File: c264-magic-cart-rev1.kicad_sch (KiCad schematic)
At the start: 10 parts, among them CN1 C16_NEWSTYLE_EXP_PORT, U1 27C080, U2 74HCT273, U3 27C160, U5 GAL20V8

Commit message: Add cap for U3
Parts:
- added C3: 100n, Capacitor_THT:C_Disc_D7.5mm_W2.5mm_P5.00mm, symbol Device:C
- renumbered C2 to C1, C3 to C2
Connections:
- net GND: now also C3.2
- net VCC: now also C3.1
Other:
- moved on the sheet: C2
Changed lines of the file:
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@@
 	)
 	(junction
-		(at 218.44 127)
+		(at 46.99 175.26)
 		(diameter 0)
 		(color 0 0 0 0)
 	)
 	(junction
-		(at 88.9 177.8)
+		(at 218.44 127)
 		(diameter 0)
 		(color 0 0 0 0)
 	)
 	(junction
-		(at 35.56 175.26)
+		(at 46.99 167.64)
 		(diameter 0)
 		(color 0 0 0 0)
 	)
 	(junction
-		(at 49.53 175.26)
+		(at 88.9 177.8)
 		(diameter 0)
 		(color 0 0 0 0)
 	)
 	(junction
-		(at 49.53 167.64)
+		(at 35.56 175.26)
 		(diameter 0)
 		(color 0 0 0 0)
@@
 	(wire
 		(pts
-			(xy 35.56 175.26) (xy 49.53 175.26)
+			(xy 46.99 167.64) (xy 49.53 167.64)
+		)
+		(stroke
+			(width 0)
+			(type default)
+		)
+	)
+	(wire
+		(pts
+			(xy 35.56 175.26) (xy 46.99 175.26)
 		)
 		(stroke
@@
 	(wire
 		(pts
-			(xy 49.53 175.26) (xy 54.61 175.26)
-		)
-		(stroke
-			(width 0.1524)
-			(type solid)
-		)
-	)
-	(wire
-		(pts
 			(xy 81.28 113.03) (xy 83.82 113.03)
 		)
@@
 	(wire
 		(pts
-			(xy 49.53 167.64) (xy 54.61 167.64)
+			(xy 49.53 167.64) (xy 58.42 167.64)
 		)
 		(stroke
@@
 	(wire
 		(pts
-			(xy 35.56 167.64) (xy 49.53 167.64)
+			(xy 35.56 167.64) (xy 46.99 167.64)
 		)
 		(stroke
@@
 	(wire
 		(pts
-			(xy 35.56 175.26) (xy 49.53 175.26)
+			(xy 35.56 175.26) (xy 46.99 175.26)
 		)
 		(stroke
@@
 	(wire
 		(pts
+			(xy 46.99 175.26) (xy 49.53 175.26)
+		)
+		(stroke
+			(width 0)
+			(type default)
+		)
+	)
+	(wire
+		(pts
 			(xy 148.59 106.68) (xy 151.13 106.68)
 		)
@@
 	(wire
 		(pts
+			(xy 46.99 175.26) (xy 58.42 175.26)
+		)
+		(stroke
+			(width 0.1524)
+			(type solid)
+		)
+	)
+	(wire
+		(pts
 			(xy 123.19 116.84) (xy 120.65 116.84)
 		)
@@
 	(symbol
 		(lib_id "Device:C")
-		(at 49.53 171.45 0)
+		(at 46.99 171.45 0)
 		(unit 1)
 		(exclude_from_sim no)
@@
 		(dnp no)
 		(fields_autoplaced yes)
-		(property "Reference" "C3"
-			(at 53.34 170.1799 0)
+		(property "Reference" "C2"
+			(at 50.8 170.1799 0)
 			(effects
 				(font
@@
 		)
 		(property "Value" "100n"
-			(at 53.34 172.7199 0)
+			(at 50.8 172.7199 0)
 			(effects
 				(font
@@
 		)
 		(property "Footprint" "Capacitor_THT:C_Disc_D7.5mm_W2.5mm_P5.00mm"
-			(at 50.4952 175.26 0)
+			(at 47.9552 175.26 0)
 			(effects
 				(font
@@
 		)
 		(property "Datasheet" "~"
-			(at 49.53 171.45 0)
+			(at 46.99 171.45 0)
 			(effects
 				(font
@@
 		)
 		(property "Description" "Unpolarized capacitor"
-			(at 49.53 171.45 0)
+			(at 46.99 171.45 0)
 			(effects
 				(font
@@
 			(project "c264-magic-cart-rev1"
 				(path "/4f6144cc-f8fb-4506-9c6e-a7a5c74469ea"
-					(reference "C3")
+					(reference "C2")
 					(unit 1)
 				)
@@
 		(dnp no)
 		(fields_autoplaced yes)
-		(property "Reference" "C2"
+		(property "Reference" "C1"
 			(at 39.37 170.1799 0)
 			(effects
@@
 			(project ""
 				(path "/4f6144cc-f8fb-4506-9c6e-a7a5c74469ea"
-					(reference "C2")
+					(reference "C1")
 					(unit 1)
 				)
@@
 					(unit 1)
 				)
+			)
+		)
+	)
+	(symbol
+		(lib_id "Device:C")
+		(at 58.42 171.45 0)
+		(unit 1)
+		(exclude_from_sim no)
+		(in_bom yes)
+		(on_board yes)
+		(dnp no)
+		(fields_autoplaced yes)
+		(property "Reference" "C3"
+			(at 62.23 170.1799 0)
+			(effects
+				(font
+					(size 1.27 1.27)
+				)
+				(justify left)
+			)
+		)
+		(property "Value" "100n"
+			(at 62.23 172.7199 0)
+			(effects
+				(font
+					(size 1.27 1.27)
+				)
+				(justify left)
+			)
+		)
+		(property "Footprint" "Capacitor_THT:C_Disc_D7.5mm_W2.5mm_P5.00mm"
+			(at 59.3852 175.26 0)
+			(effects
+				(font
+					(size 1.27 1.27)
+				)
+				(hide yes)
+			)
+		)
+		(property "Datasheet" "~"
+			(at 58.42 171.45 0)
+			(effects
+				(font
+					(size 1.27 1.27)
+				)
+				(hide yes)
+			)
+		)
+		(property "Description" "Unpolarized capacitor"
+			(at 58.42 171.45 0)
+			(effects
+				(font
+					(size 1.27 1.27)
+				)
+				(hide yes)
+			)
+		)
+		(pin "1"
+		)
+		(pin "2"
+		)
+		(instances
+			(project "c264-magic-cart-rev1"
+				(path "/4f6144cc-f8fb-4506-9c6e-a7a5c74469ea"
+					(reference "C3")
+					(unit 1)
+				)

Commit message: Update silkscreen
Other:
- company: (none) -> SukkoPera
- title: (none) -> c264-magic-cart (44-Pin Version)
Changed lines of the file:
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@@
 	(paper "A4")
 	(title_block
+		(title "c264-magic-cart (44-Pin Version)")
 		(date "2026-07-27")
+		(rev "1s")
+		(company "SukkoPera")
+		(comment 1 "Licensed under CERN OHL v.1.2")
+		(comment 2 "https://github.com/SukkoPera/c264-magic-cart-44pin")
 	)
 	(junction

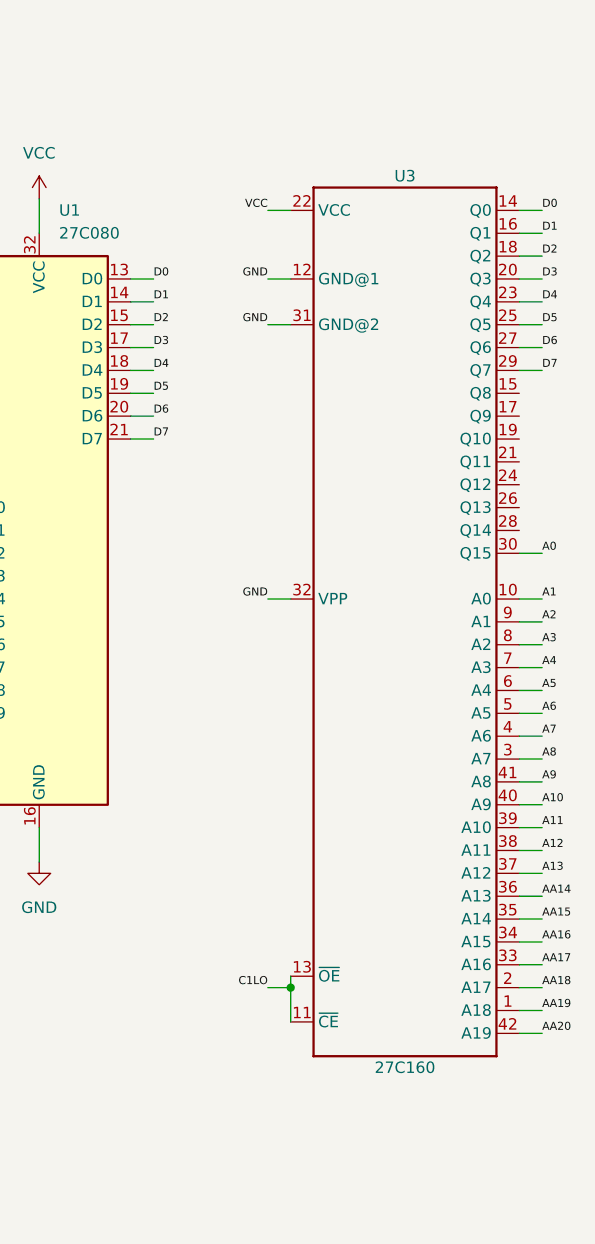
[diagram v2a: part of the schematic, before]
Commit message: Get rid of unused footprints
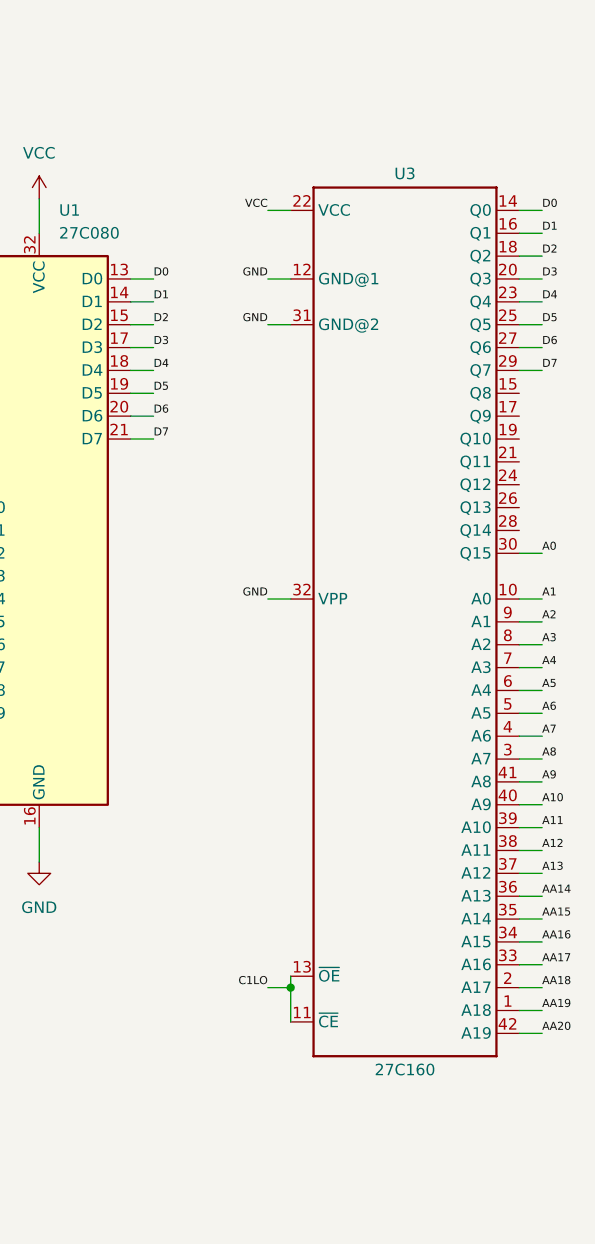
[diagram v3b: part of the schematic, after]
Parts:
- removed U3: 27C160, Package_DIP:DIP-42_W15.24mm_Socket, symbol c264-magic-cart-rev1-eagle-import:27C160_DIP42
- added U3: 27C160, Package_DIP:DIP-42_W15.24mm_Socket, symbol 27c160_dip42:27C160_DIP42
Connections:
- net A0: now also U3.30 (Q15)
- net A1: now also U3.10 (A0)
- net A10: now also U3.40 (A9)
- net A11: now also U3.39 (A10)
- net A12: now also U3.38 (A11)
- net A13: now also U3.37 (A12)
- net A2: now also U3.9 (A1)
- net A3: now also U3.8 (A2)
- net A4: now also U3.7 (A3)
- net A5: now also U3.6 (A4)
- net A6: now also U3.5 (A5)
- net A7: now also U3.4 (A6)
- net A8: now also U3.3 (A7)
- net A9: now also U3.41 (A8)
- net AA14: now also U3.36 (A13)
- net AA15: now also U3.35 (A14)
- net AA16: now also U3.34 (A15)
- net AA17: now also U3.33 (A16)
- net AA18: now also U3.2 (A17)
- net AA19: now also U3.1 (A18)
- net AA20: now also U3.42 (A19)
- net C1LO: now also U3.11 (~{CE}), U3.13 (~{OE})
- net D0: now also U3.14 (Q0)
- net D1: now also U3.16 (Q1)
- net D2: now also U3.18 (Q2)
- net D3: now also U3.20 (Q3)
- net D4: now also U3.23 (Q4)
- net D5: now also U3.25 (Q5)
- net D6: now also U3.27 (Q6)
- net D7: now also U3.29 (Q7)
- net GND: now also U3.12 (GND@1), U3.31 (GND@2), U3.32 (VPP)
- net VCC: now also U3.22 (VCC)
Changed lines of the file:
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@@
-	)
-	(symbol
-		(lib_id "c264-magic-cart-rev1-eagle-import:27C160_DIP42")
-		(at 231.14 86.36 0)
-		(unit 1)
-		(exclude_from_sim no)
-		(in_bom yes)
-		(on_board yes)
-		(dnp no)
-		(property "Reference" "U3"
-			(at 231.14 36.83 0)
-			(effects
-				(font
-					(size 1.27 1.27)
-					(thickness 0.1588)
-				)
-			)
-		)
-		(property "Value" "27C160"
-			(at 231.14 135.89 0)
-			(effects
-				(font
-					(size 1.27 1.27)
-					(thickness 0.1588)
-				)
-			)
-		)
-		(property "Footprint" "Package_DIP:DIP-42_W15.24mm_Socket"
-			(at 231.14 86.36 0)
-			(effects
-				(font
-					(size 1.27 1.27)
-				)
-				(hide yes)
-			)
-		)
-		(property "Datasheet" ""
-			(at 231.14 86.36 0)
-			(effects
-				(font
-					(size 1.27 1.27)
-				)
-				(hide yes)
-			)
-		)
-		(property "Description" ""
-			(at 231.14 86.36 0)
-			(effects
-				(font
-					(size 1.27 1.27)
-				)
-				(hide yes)
-			)
-		)
-		(pin "1"
-		)
-		(pin "10"
-		)
-		(pin "11"
-		)
-		(pin "12"
-		)
-		(pin "13"
-		)
-		(pin "14"
-		)
-		(pin "15"
-		)
-		(pin "16"
-		)
-		(pin "17"
-		)
-		(pin "18"
-		)
-		(pin "19"
-		)
-		(pin "2"
-		)
-		(pin "20"
-		)
-		(pin "21"
-		)
-		(pin "22"
-		)
-		(pin "23"
-		)
-		(pin "24"
-		)
-		(pin "25"
-		)
-		(pin "26"
-		)
-		(pin "27"
-		)
-		(pin "28"
-		)
-		(pin "29"
-		)
-		(pin "3"
-		)
-		(pin "30"
-		)
-		(pin "31"
-		)
-		(pin "32"
-		)
-		(pin "33"
-		)
-		(pin "34"
-		)
-		(pin "35"
-		)
-		(pin "36"
-		)
-		(pin "37"
-		)
-		(pin "38"
-		)
-		(pin "39"
-		)
-		(pin "4"
-		)
-		(pin "40"
-		)
-		(pin "41"
-		)
-		(pin "42"
-		)
-		(pin "5"
-		)
-		(pin "6"
-		)
-		(pin "7"
-		)
-		(pin "8"
-		)
-		(pin "9"
-		)
-		(instances
-			(project ""
-				(path "/4f6144cc-f8fb-4506-9c6e-a7a5c74469ea"
-					(reference "U3")
-					(unit 1)
-				)
-			)
-		)
 	)
 	(symbol
@@
 					(unit 1)
 				)
+			)
+		)
+	)
+	(symbol
+		(lib_id "27c160_dip42:27C160_DIP42")
+		(at 231.14 86.36 0)
+		(unit 1)
+		(exclude_from_sim no)
+		(in_bom yes)
+		(on_board yes)
+		(dnp no)
+		(property "Reference" "U3"
+			(at 231.14 36.576 0)
+			(effects
+				(font
+					(size 1.27 1.27)
+					(thickness 0.1588)
+				)
+			)
+		)
+		(property "Value" "27C160"
+			(at 231.14 136.144 0)
+			(effects
+				(font
+					(size 1.27 1.27)
+					(thickness 0.1588)
+				)
+			)
+		)
+		(property "Footprint" "Package_DIP:DIP-42_W15.24mm_Socket"
+			(at 231.14 86.36 0)
+			(effects
+				(font
+					(size 1.27 1.27)
+				)
+				(hide yes)
+			)
+		)
+		(property "Datasheet" ""
+			(at 231.14 86.36 0)
+			(effects
+				(font
+					(size 1.27 1.27)
+				)
+				(hide yes)
+			)
+		)
+		(property "Description" ""
+			(at 231.14 86.36 0)
+			(effects
+				(font
+					(size 1.27 1.27)
+				)
+				(hide yes)
+			)
+		)
+		(pin "12"
+		)
+		(pin "34"
+		)
+		(pin "15"
+		)
+		(pin "42"
+		)
+		(pin "5"
+		)
+		(pin "17"
+		)
+		(pin "14"
+		)
+		(pin "11"
+		)
+		(pin "40"
+		)
+		(pin "41"
+		)
+		(pin "16"
+		)
+		(pin "35"
+		)
+		(pin "36"
+		)
+		(pin "18"
+		)
+		(pin "8"
+		)
+		(pin "9"
+		)
+		(pin "23"
+		)
+		(pin "37"
+		)
+		(pin "38"
+		)
+		(pin "6"
+		)
+		(pin "7"
+		)
+		(pin "21"
+		)
+		(pin "31"
+		)
+		(pin "26"
+		)
+		(pin "20"
+		)
+		(pin "30"
+		)
+		(pin "39"
+		)
+		(pin "4"
+		)
+		(pin "28"
+		)
+		(pin "2"
+		)
+		(pin "19"
+		)
+		(pin "3"
+		)
+		(pin "25"
+		)
+		(pin "13"
+		)
+		(pin "22"
+		)
+		(pin "32"
+		)
+		(pin "33"
+		)
+		(pin "27"
+		)
+		(pin "29"
+		)
+		(pin "1"
+		)
+		(pin "10"
+		)
+		(pin "24"
+		)
+		(instances
+			(project ""
+				(path "/4f6144cc-f8fb-4506-9c6e-a7a5c74469ea"
+					(reference "U3")
+					(unit 1)
+				)

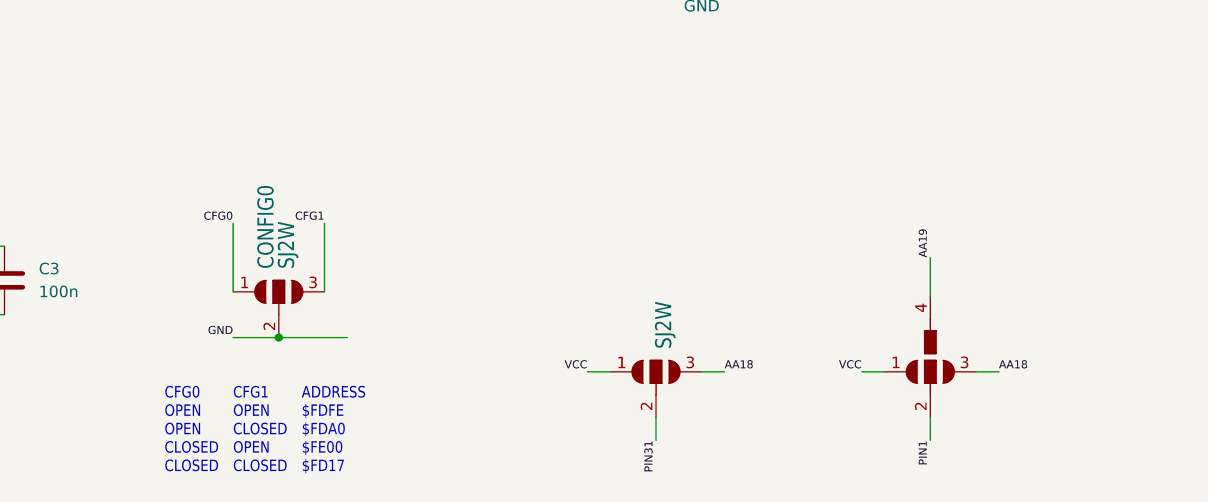
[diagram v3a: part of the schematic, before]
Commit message: Get rid of jumper footprints
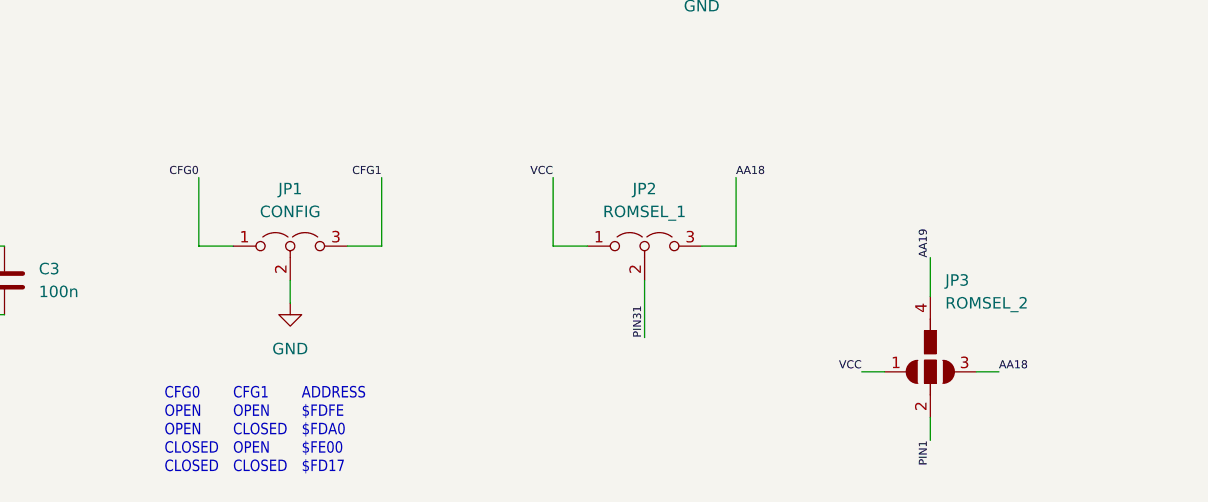
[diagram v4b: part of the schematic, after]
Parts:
- removed CONFIG0: SJ2W, c264-magic-cart-rev1:SJ_2, symbol c264-magic-cart-rev1-eagle-import:SJ2W
- removed SJ1: SJ2W, c264-magic-cart-rev1:SJ_2, symbol c264-magic-cart-rev1-eagle-import:jumper-edit_SJ2W
- added JP1: CONFIG, Jumper:SolderJumper-3_P1.3mm_Open_Pad1.0x1.5mm, symbol Jumper:Jumper_3_Open
- added JP2: ROMSEL_1, Jumper:SolderJumper-3_P1.3mm_Open_Pad1.0x1.5mm, symbol Jumper:Jumper_3_Open
- JP3: renamed from U$2; value SJ3 -> ROMSEL_2
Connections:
- net AA18: now also JP2.3 (B)
- net CFG0: now also JP1.1 (A)
- net CFG1: now also JP1.3 (B)
- net GND: now also JP1.2 (C)
- net PIN31: now also JP2.2 (C)
- net VCC: now also JP2.1 (A)

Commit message: Add bank selection jumpers
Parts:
- added JP4, JP5: CONFIG, Jumper:SolderJumper-3_P1.3mm_Open_Pad1.0x1.5mm, symbol Jumper:Jumper_3_Open
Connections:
- net C1LO: now also JP4.1 (A), JP5.1 (A); no longer U1.22 (~{CE}), U1.24 (~{OE}), U3.11 (~{CE}), U3.13 (~{OE})
- net ~{cs0}: now reaches CN1.10 (~{CS0})
- net ~{cs0}: now also JP4.3 (B)
- net ~{c2}: now reaches CN1.D (~{C2})
- net ~{c2}: now also JP5.3 (B)
- new net rom_ce: JP4.2 (C), U1.22 (~{CE}), U3.11 (~{CE})
- new net rom_oe: JP5.2 (C), U1.24 (~{OE}), U3.13 (~{OE})
- no-connect marks 11 -> 16
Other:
- note added: "SELECTS BYTE-WISE OPERATION"
